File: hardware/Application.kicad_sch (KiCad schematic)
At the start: 29 parts, among them J501 Conn_ARM_SWD_TagConnect_TC203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, J502 Conn_ARM_SWD_TagConnect_TC2030, J503 BOOT0, U501 STM32G431CBU6, Y501 32_Mhz

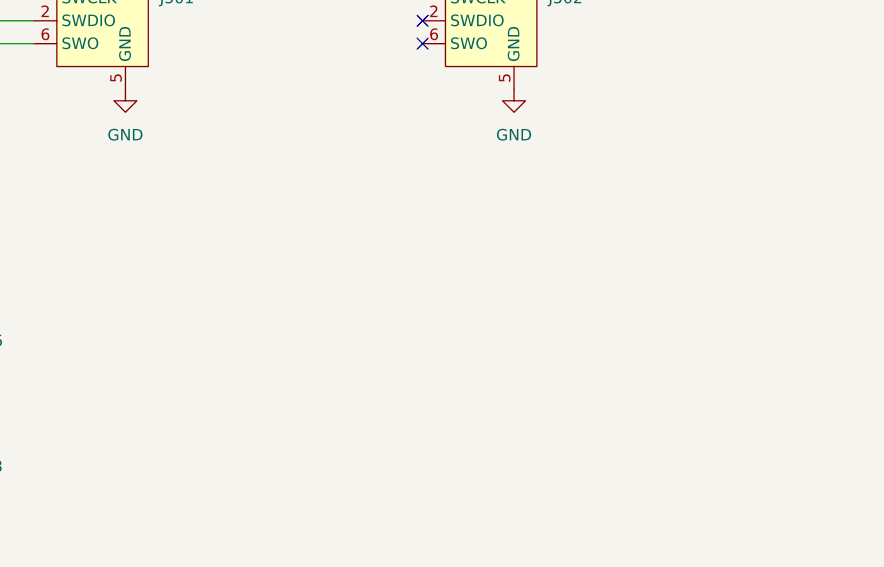
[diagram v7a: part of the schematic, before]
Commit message: hardware: Add flash storage
Signed-off-by: Connor Rigby <connorr@hey.com>
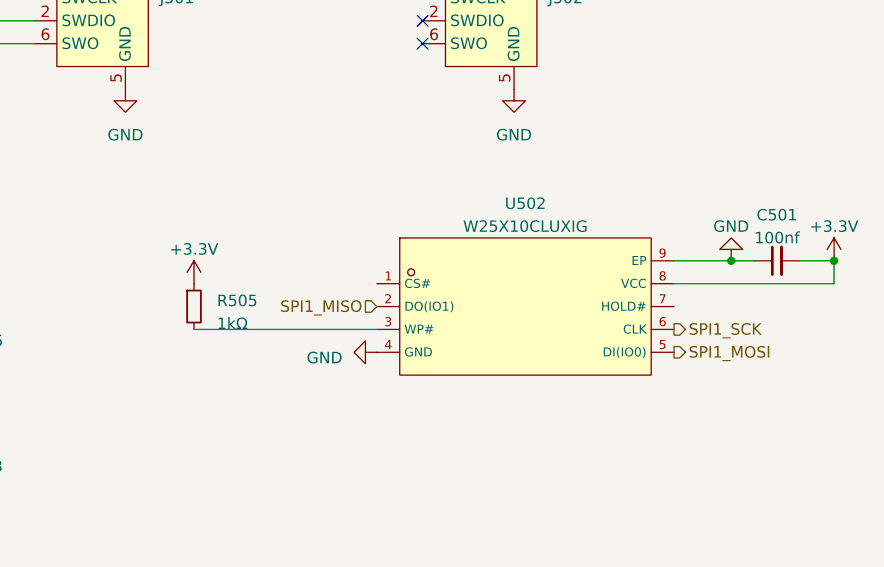
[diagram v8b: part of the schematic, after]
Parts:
- added C501: C_0402_100nf_X7R, Capacitor_SMD:C_0402_1005Metric, symbol LCSC_Capacitor:C_0402_100nf_X7R
- added R505: R_0402_1k, Resistor_SMD:R_0402_1005Metric, symbol LCSC_Resistor:R_0402_1k
- added U502: W25X10CLUXIG, LCSC_Microcontroller:USON-8_L3.0-W2.0-P0.50-BL-EP-1, symbol LCSC_Microcontroller:W25X10CLUXIG
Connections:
- net +3.3V: now also C501.2, R505.1, U502.8 (VCC)
- net GND: now also C501.1, U502.4 (GND), U502.9 (EP)
- net SPI1_MISO: now also U502.2 (DO(IO1))
- net SPI1_MOSI: now also U502.5 (DI(IO0))
- net SPI1_SCK: now also U502.6 (CLK)
- new net: R505.2, U502.3 (WP#)
